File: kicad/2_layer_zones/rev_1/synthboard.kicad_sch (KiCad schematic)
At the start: 51 parts, among them J1 Connection to Upper Module/FP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, J2 Connection to Lower Module, J3 Modular Inputs, SW1 SW_Push, SW10 SW_Push, SW11 SW_Push, SW12 SW_Push, SW2 SW_Push, SW3 SW_Push, SW4 SW_Push, SW5 SW_Push, SW6 SW_Push, SW7 SW_Push, SW8 SW_Push, SW9 SW_Push, U1 74HC165, U2 74HC165

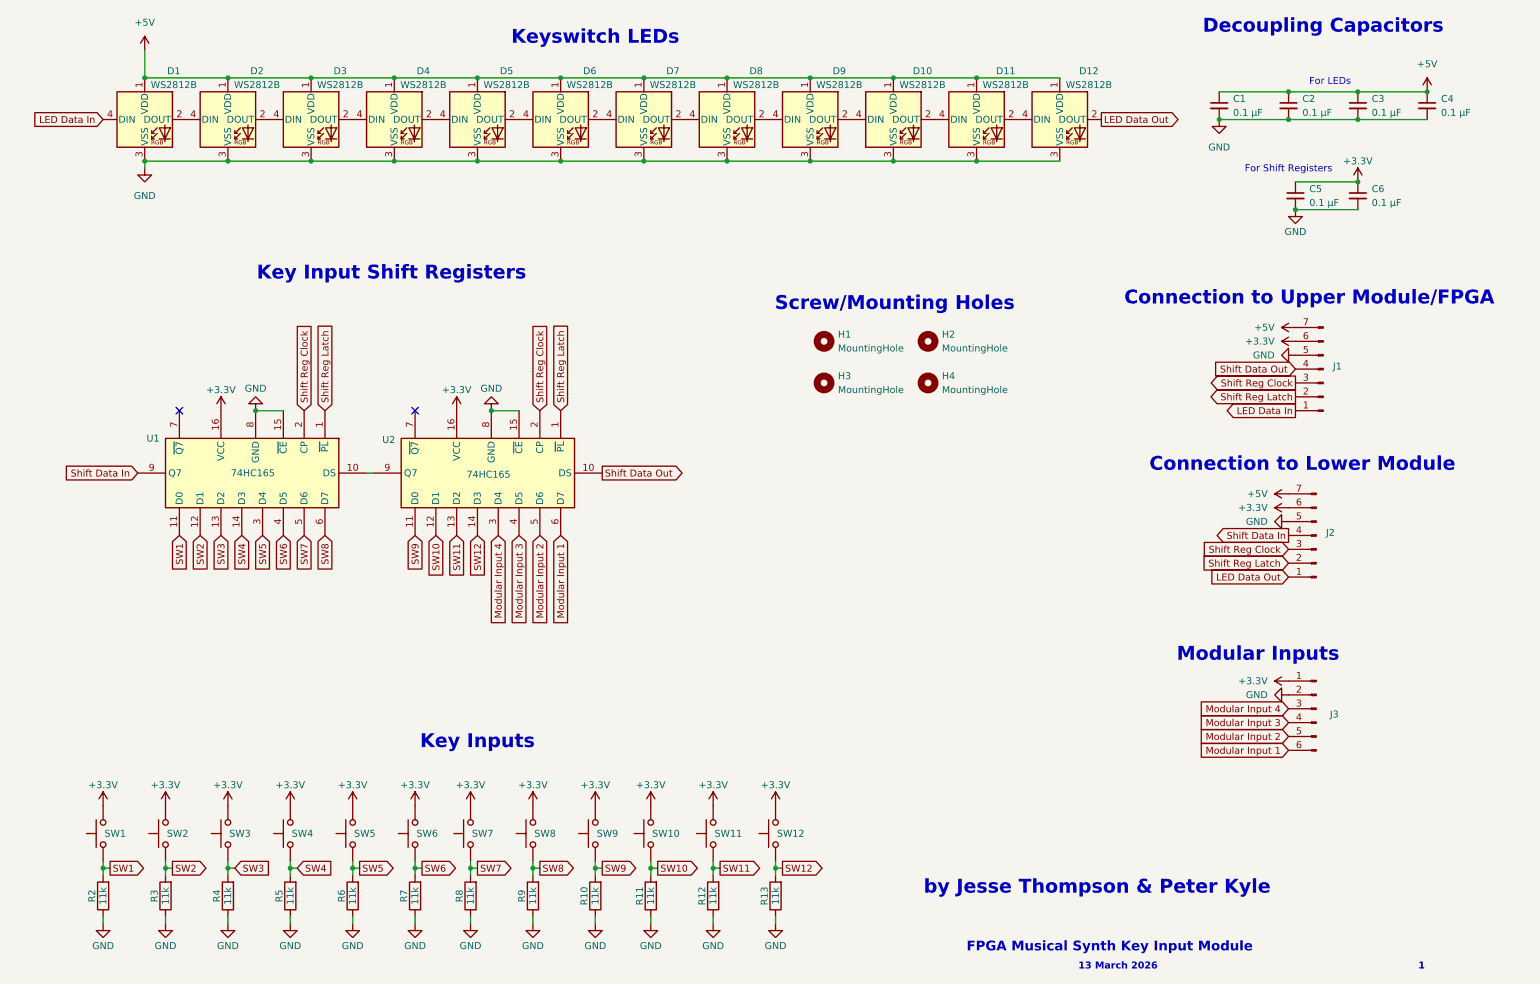
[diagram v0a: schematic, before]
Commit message: 2 layer board edits
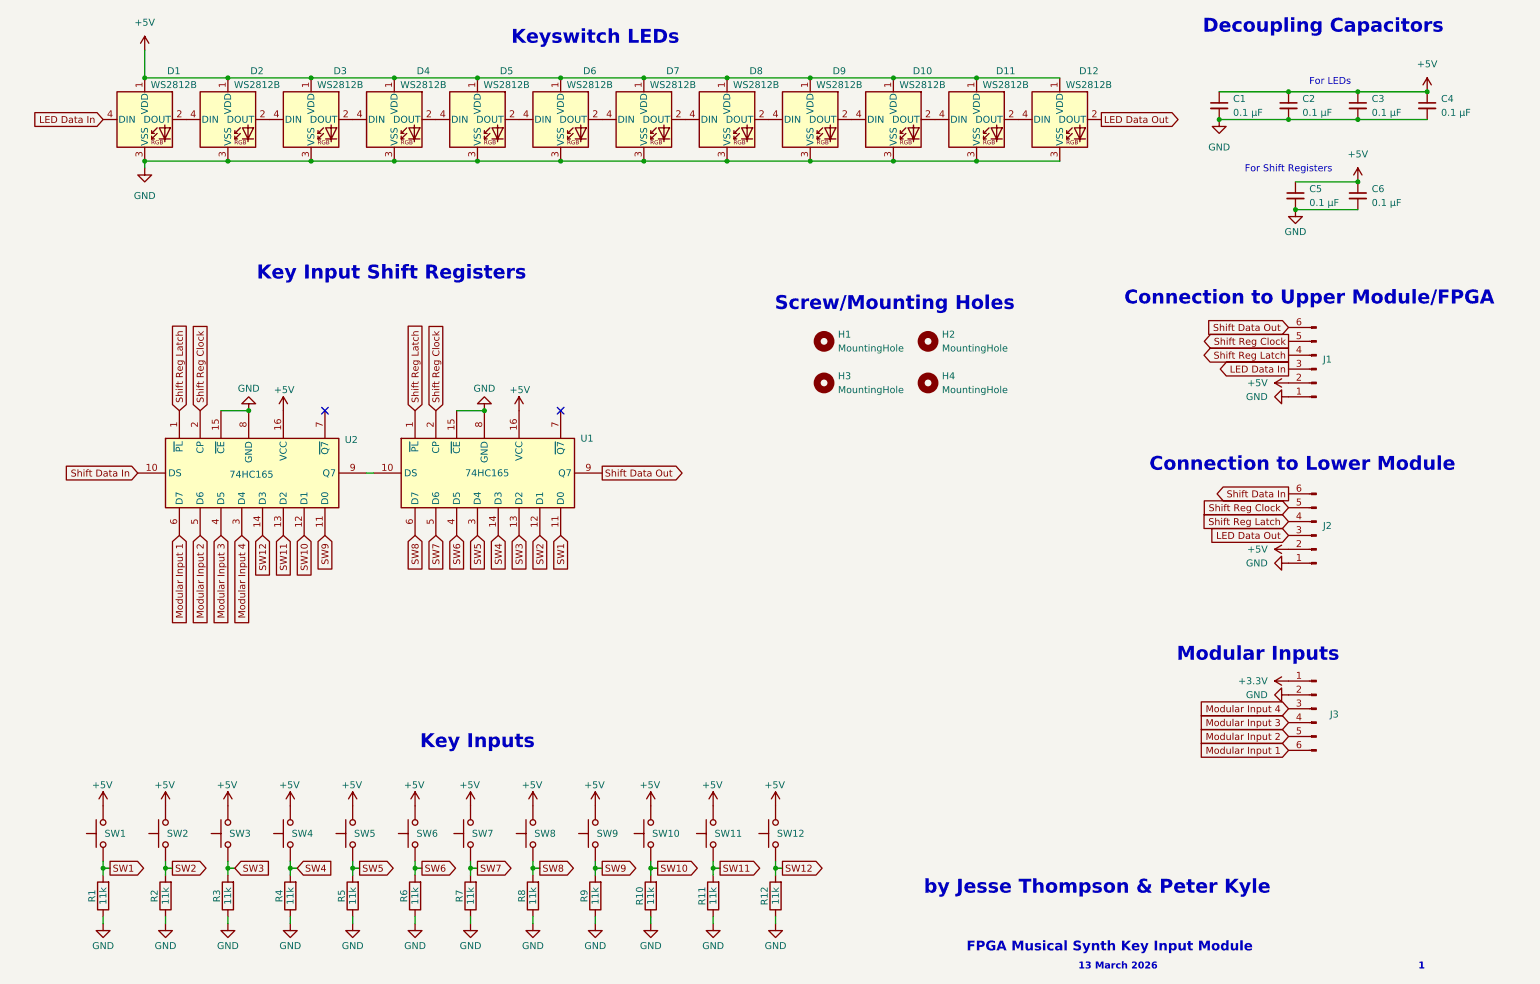
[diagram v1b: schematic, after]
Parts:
- removed J1: Connection to Upper Module/FPGA, Connector_PinHeader_2.54mm:PinHeader_1x07_P2.54mm_Vertical, symbol Connector:Conn_01x07_Pin
- removed J2: Connection to Lower Module, Connector_PinHeader_2.54mm:PinHeader_1x07_P2.54mm_Vertical, symbol Connector:Conn_01x07_Pin
- added J1: Connect to Upper Module/Motherboard, Connector_PinSocket_2.54mm:PinSocket_1x06_P2.54mm_Horizontal, symbol Connector:Conn_01x06_Pin
- added J2: Connect to Lower Module, Connector_PinSocket_2.54mm:PinSocket_1x06_P2.54mm_Vertical, symbol Connector:Conn_01x06_Pin
- renumbered R2 to R1, R11 to R10, R12 to R11, R13 to R12, R3 to R2, R4 to R3, R5 to R4, R6 to R5, R7 to R6, R8 to R7, R9 to R8, R10 to R9
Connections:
- net +3.3V: no longer C5.1, C6.1, SW1.2, SW10.2, SW11.2, SW12.2, SW2.2, SW3.2, SW4.2, SW5.2, SW6.2, SW7.2, SW8.2, SW9.2, U1.16 (VCC), U2.16 (VCC)
- net +5V: now also C5.1, C6.1, SW1.2, SW10.2, SW11.2, SW12.2, SW2.2, SW3.2, SW4.2, SW5.2, SW6.2, SW7.2, SW8.2, SW9.2, U1.16 (VCC), U2.16 (VCC), J1.2 (Pin_2), J2.2 (Pin_2)
- net GND: now also J1.1 (Pin_1), J2.1 (Pin_1)
- net LED Data In: now also J1.3 (Pin_3)
- net LED Data Out: now also J2.3 (Pin_3)
- net Shift Data In: now also U2.10 (DS), J2.6 (Pin_6); no longer U1.9 (Q7)
- net Shift Data Out: now also U1.9 (Q7), J1.6 (Pin_6); no longer U2.10 (DS)
- net Shift Reg Clock: now also J1.5 (Pin_5), J2.5 (Pin_5)
- net Shift Reg Latch: now also J1.4 (Pin_4), J2.4 (Pin_4)
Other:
- moved on the sheet: U1, U2
